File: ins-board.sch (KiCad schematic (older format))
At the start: 76 parts, among them P1 PWR, P2 Power (Solder Pad), Q1 FDN306P, Q2 FDC638APZ, U1 24LC128, U2 STM32F415RGT6, U3 LTC4412, U4 MAX3051, U5 LT1965, U6 LT1761-3.3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

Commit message: start fixing schematic
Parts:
- removed D6: BAS52-02V, symbol DIODESCH
- added D6: BAS52-02V, symbol D_Schottky
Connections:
- wire segments 154 -> 221
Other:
- moved on the sheet: C1, C10, C11, C12, C13, C14, C2, C3, C5, C6, C7, C8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

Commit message: reorganize schematic
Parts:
- removed C17: 0.1uF, symbol C
- removed C20, C23: 10uF, symbol C
- removed CONN4: I2C/UART, MODULE, symbol I2C
- removed D6: BAS52-02V, symbol D_Schottky
- removed P1: PWR, MODULE, symbol PWR
- removed P2: Power (Solder Pad), ~, symbol CONN_2
- removed Q2: FDC638APZ, symbol MOS_P
- removed R16, R17: 4.7k, symbol R
- removed R18: NP / 120, symbol R
- removed R20: 47k, symbol R
- removed U3: LTC4412, MODULE, symbol LTC4412
- removed U5: LT1965, MODULE, symbol LT1965
- added C?: 100nF, symbol C
- added C?: 0.1uF, ~, symbol C
- added CONN? (x3): CAN, MODULE, symbol CAN
- added D? (x3): BAS52-02V, symbol D_Schottky
- added D?: TVS, symbol TVS
- added R?: 0, symbol R
- added U?: MAX3051, MODULE, symbol MAX3051
- R5: value 10k -> 100k
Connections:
- net labels added: V_BUS1, V_BUS2
- wire segments 221 -> 165
- no-connect marks 5 -> 4
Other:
- note removed: "3.6V...20V"
- note removed: "ideal diode controller"
- moved on the sheet: C13, C18, C19, C21, C22, C24, C25, C26, C27, C4, CONN3, CONN5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

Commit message: power supply
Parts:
- removed D? (x2): BAS52-02V, symbol D_Schottky
- removed F1: FUSE 500mA, symbol FUSE
- added D? (x2): BAS52-02V, symbol D_Schottky
- added D? (x2): TVS, symbol TVS
- added D?: ZENERsmall, symbol ZENERsmall
- added F?: 200mA, symbol F_Small
- added F? (x3): 500mA, symbol F_Small
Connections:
- net labels added: 5V_MON_AD
- net labels removed: V_DC
- wire segments 165 -> 177
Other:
- note added: "TPS25200"
- moved on the sheet: C15, C16, C18, C22, C26, C4, D2, D?, R10, R11, R21, R3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

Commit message: fuses & diodes
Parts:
- removed F?: 200mA, symbol F_Small
- removed F? (x2): 500mA, symbol F_Small
- added F? (x2): 500mA, symbol F_Small
- added F?: 200mA, symbol F_Small
- D? (x3): value BAS52-02V -> SBR130S3-7
- D?: value ZENERsmall -> TVS
- F?: Part (none) -> 0ZCK0050FF2E
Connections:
- wire segments 177 -> 240
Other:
- moved on the sheet: C18, C21, C22, C24, C25, C26, C27, FB1, R21, U6, U7

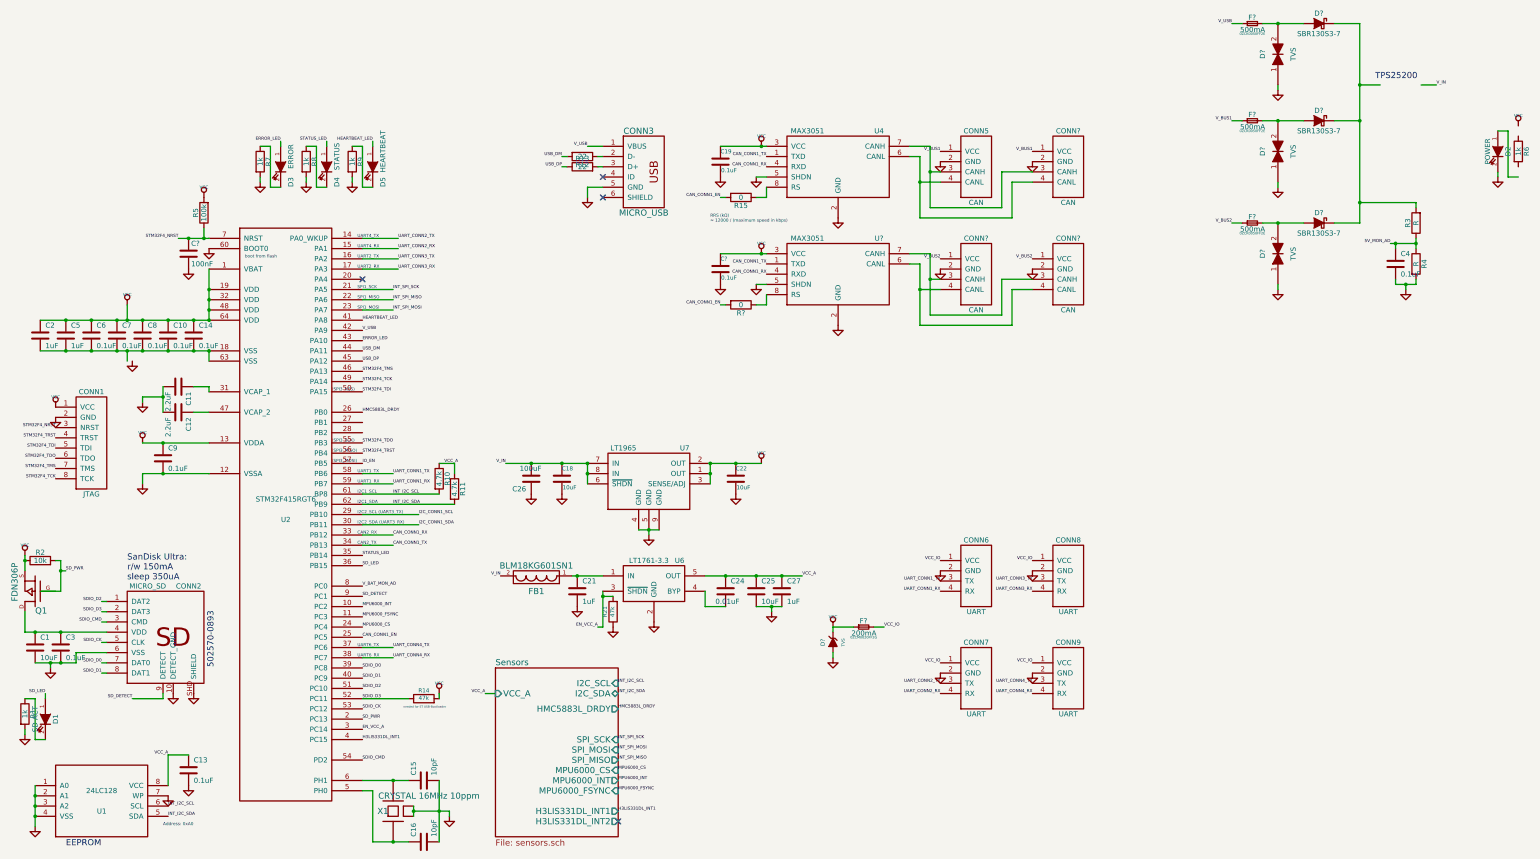
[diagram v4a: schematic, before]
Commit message: add FRAM
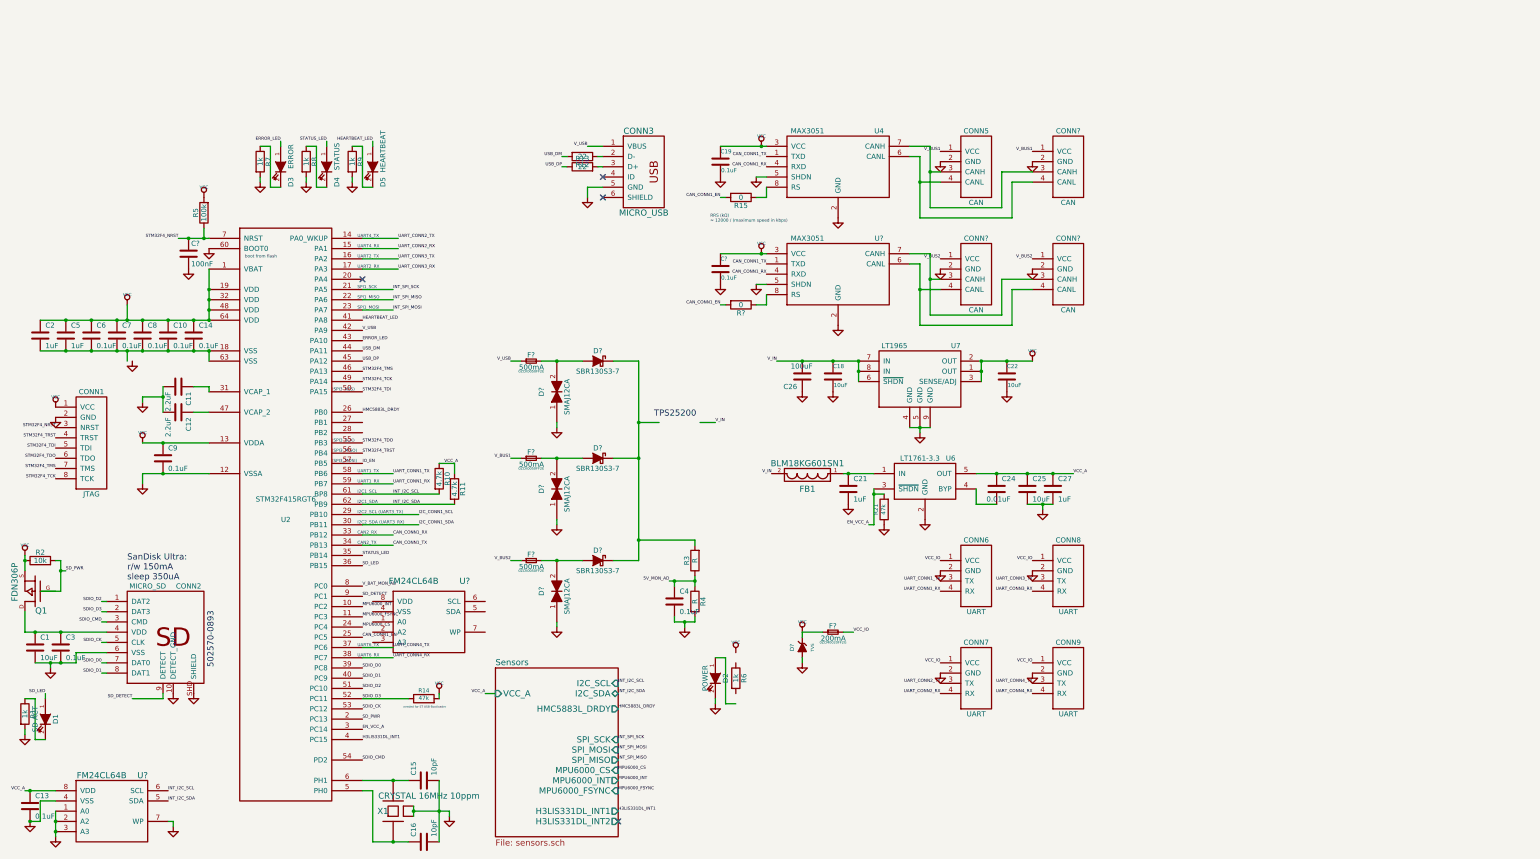
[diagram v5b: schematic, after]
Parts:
- removed U1: 24LC128, MODULE, symbol 24LC128
- added U? (x2): FM24CL64B, symbol FM24CL64B
- D? (x3): value TVS -> SMAJ12CA
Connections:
- net GND: now also U?.1 (A0), U?.2 (A2), U?.3 (A3), U?.4 (VSS), U?.7 (WP)
- net INT_I2C_SCL: now also U?.6 (SCL)
- net INT_I2C_SDA: now also U?.5 (SDA)
- net VCC_A: now also U?.8 (VDD)
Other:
- note removed: "Address: 0xA0"
- note removed: "EEPROM"
- moved on the sheet: C13, C18, C21, C22, C24, C25, C26, C27, C4, D2, D?, F?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

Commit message: schematic organization
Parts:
- removed U?: FM24CL64B, symbol FM24CL64B
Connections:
- net GND: now also R6.2; no longer D2.2 (K)
- net VCC: now also D2.1 (A)
- net at R6.1: now also D2.2 (K)
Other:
- moved on the sheet: C1, C10, C11, C12, C13, C14, C15, C16, C18, C2, C21, C22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

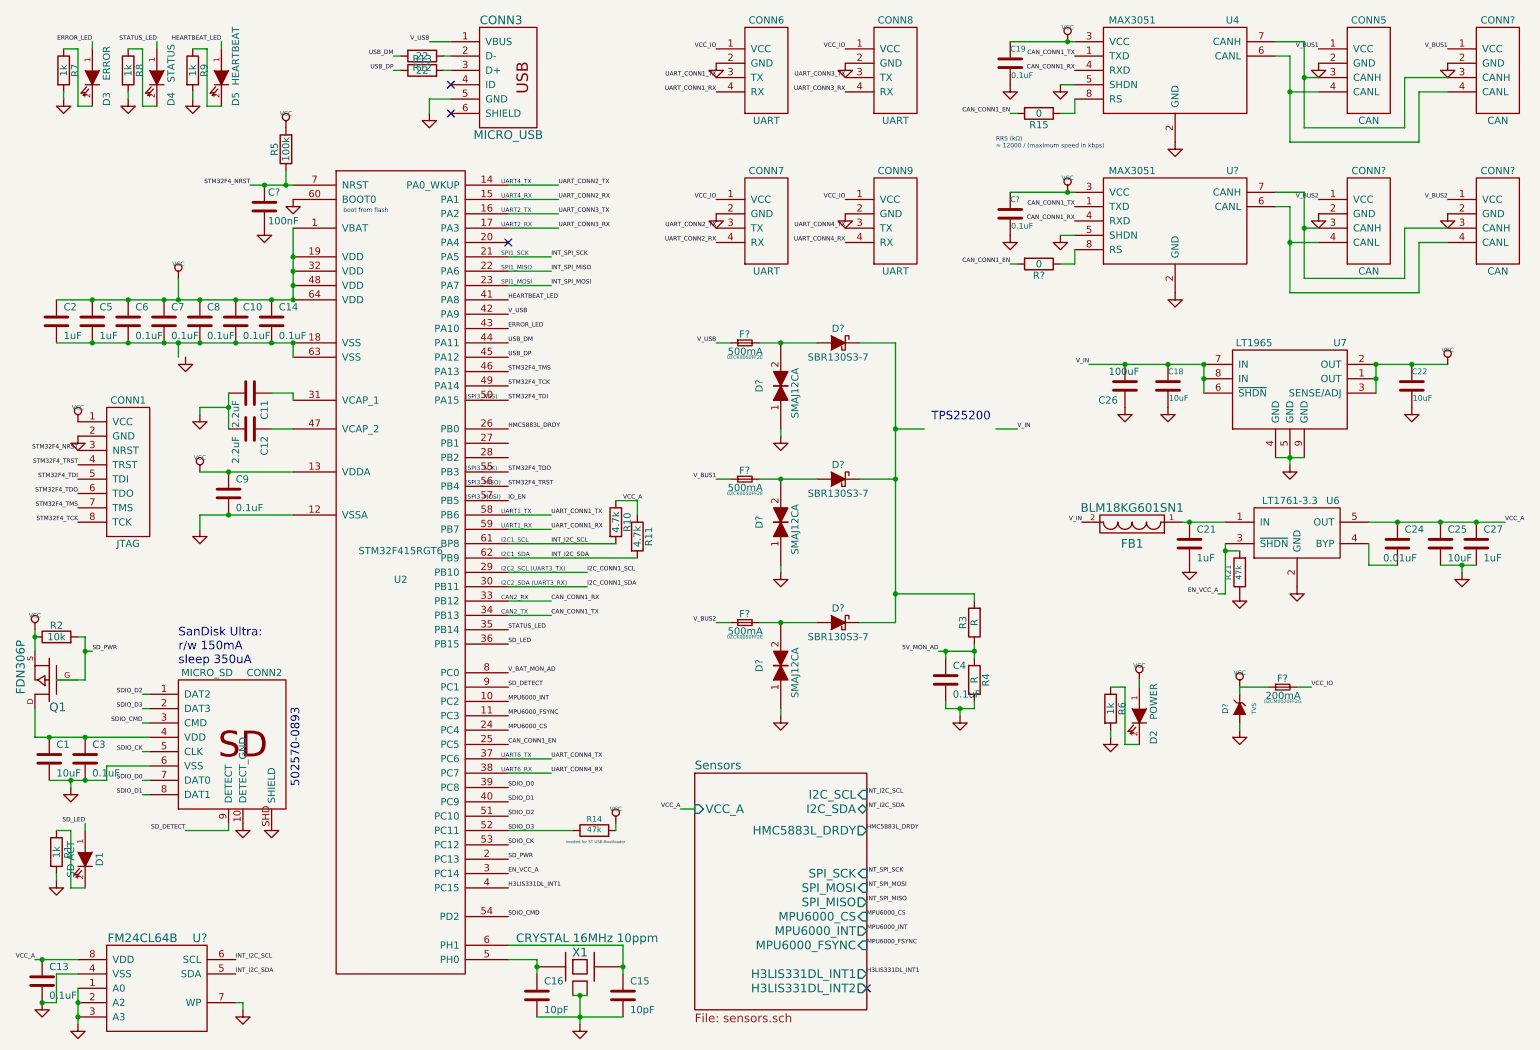
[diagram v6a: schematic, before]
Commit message: schematic layout
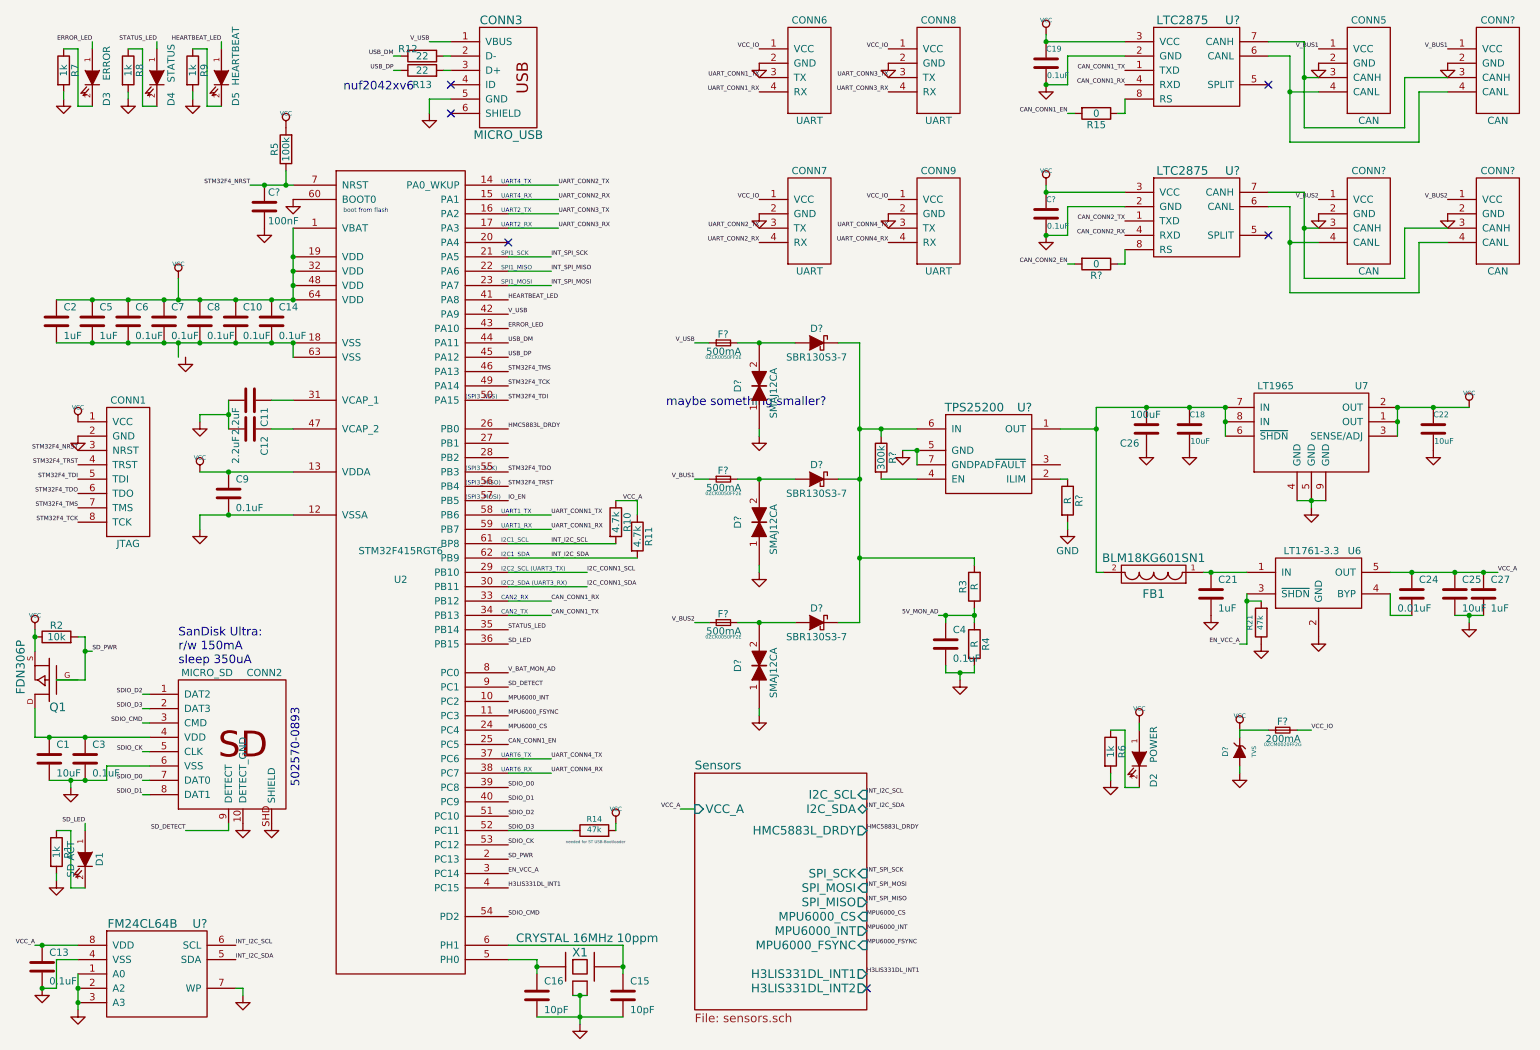
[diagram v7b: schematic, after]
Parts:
- removed C?: 0.1uF, ~, symbol C
- removed R?: 0, symbol R
- removed U4, U?: MAX3051, MODULE, symbol MAX3051
- added C?: 0.1uF, ~, symbol C
- added R?: 0, symbol R
- added R?: R, symbol R
- added R?: 300k, symbol R
- added U? (x2): LTC2875, symbol LTC2875
- added U?: TPS25200, symbol TPS25200
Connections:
- net CAN_CONN1_RX: now also U?.4 (RXD)
- net CAN_CONN1_TX: now also U?.1 (TXD)
- net GND: now also C?.2, R?.2, U?.2 (GND), U?.2 (GND), U?.5 (GND), U?.7 (GNDPAD)
- net VCC: now also C?.1, U?.3 (VCC), U?.3 (VCC)
- net at CONN5.3 (CANH), CONN?.3 (CANH): now also U?.7 (CANH)
- net at CONN5.4 (CANL), CONN?.4 (CANL): now also U?.6 (CANL)
- net at R15.1: now also U?.8 (RS)
- net at D?.2 (K), D?.2 (K), D?.2 (K)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: now also R?.1, U?.6 (IN)
- net at CONN?.3 (CANH), CONN?.3 (CANH): now also U?.7 (CANH)
- net at CONN?.4 (CANL), CONN?.4 (CANL): now also U?.6 (CANL)
- net V_IN: no longer names the net of C18.1, C26.2, FB1.2, U7.6 (~SHDN), U7.7 (IN), U7.8 (IN)
- net V_IN: now also U?.1 (OUT)
- new net: R?.1, U?.8 (RS)
- new net: R?.1, U?.2 (ILIM)
- new net: R?.2, U?.4 (EN)
- new net CAN_CONN2_EN: R?.2
- new net CAN_CONN2_RX: U?.4 (RXD)
- new net CAN_CONN2_TX: U?.1 (TXD)
- no-connect marks 4 -> 6
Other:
- note added: "maybe something smaller?"
- note added: "nuf2042xv6"
- note removed: "RRS (kΩ)\n≈ 12000 / (maximum speed in kbps)"
- note removed: "TPS25200"
- moved on the sheet: C11, C13, C18, C19, C21, C22, C24, C25, C26, C27, C4, CONN6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

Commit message: power supply notes
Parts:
- removed D?: SMAJ12CA, symbol TVS
- added C?: 4.7nF 250V, symbol C
- added R?: 1M, symbol R
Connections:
- net GND: now also C?.2, R?.2
- net V_USB: now also D?.1 (A); no longer CONN3.1 (VBUS), F?.1
- net at CONN3.6 (SHIELD): now also C?.1, R?.1
- net at F?.2: now also CONN3.1 (VBUS); no longer D?.1 (A)
- no-connect marks 6 -> 5
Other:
- note added: "0.36V drop @0.5A"
- note added: "0.425V drop @0.5A"
- note added: "0.45V drop @0.5A"
- note added: "4.5V-6.5V\n0.5A"
- note removed: "maybe something smaller?"
- moved on the sheet: CONN3, D3, D4, D5, D?, F?, R12, R13, R7, R8, R9
